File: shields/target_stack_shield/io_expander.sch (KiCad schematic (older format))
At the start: 21 parts, among them U5 PCA9535CPW,118

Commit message: work on target stack shield layout
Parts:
- C7: footprint (none) -> Capacitor_SMD:C_0603_1608Metric_Pad1.05x0.95mm_HandSolder
- JP1, JP2, JP3: footprint (none) -> Jumper:SolderJumper-2_P1.3mm_Open_TrianglePad1.0x1.5mm
- LED2: footprint KRTBAILMS15B5CB1B120R18 -> hive:KRTBAILMS15B5CB1B120R18
- R10, R11, R12, R13, R14, R15, R16, R2, R3, R4, R5, R6, R7, R8, R9: footprint (none) -> Resistor_SMD:R_0603_1608Metric_Pad1.05x0.95mm_HandSolder
- U5: footprint SOP65P640X110-24N -> hive:SOP65P640X110-24N
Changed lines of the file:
@@
 F 0 "U5" H 6000 4320 50  0000 C CNN
 F 1 "PCA9535CPW,118" H 6000 4229 50  0000 C CNN
-F 2 "SOP65P640X110-24N" H 6000 3150 50  0001 L BNN
+F 2 "hive:SOP65P640X110-24N" H 6000 3150 50  0001 L BNN
 F 3 "" H 6000 3150 50  0001 L BNN
 F 4 "70R6541" H 6000 3150 50  0001 L BNN "OC_NEWARK"
@@
 F 0 "JP1" H 1600 1355 50  0000 C CNN
 F 1 "Address Bit 0" H 1600 1264 50  0000 C CNN
-F 2 "" H 1600 1150 50  0001 C CNN
+F 2 "Jumper:SolderJumper-2_P1.3mm_Open_TrianglePad1.0x1.5mm" H 1600 1150 50  0001 C CNN
 F 3 "~" H 1600 1150 50  0001 C CNN
 	1    1600 1150
@@
 F 0 "JP2" H 1600 1755 50  0000 C CNN
 F 1 "Address Bit 1" H 1600 1664 50  0000 C CNN
-F 2 "" H 1600 1550 50  0001 C CNN
+F 2 "Jumper:SolderJumper-2_P1.3mm_Open_TrianglePad1.0x1.5mm" H 1600 1550 50  0001 C CNN
 F 3 "~" H 1600 1550 50  0001 C CNN
 	1    1600 1550
@@
 F 0 "JP3" H 1600 2155 50  0000 C CNN
 F 1 "Address Bit 2" H 1600 2064 50  0000 C CNN
-F 2 "" H 1600 1950 50  0001 C CNN
+F 2 "Jumper:SolderJumper-2_P1.3mm_Open_TrianglePad1.0x1.5mm" H 1600 1950 50  0001 C CNN
 F 3 "~" H 1600 1950 50  0001 C CNN
 	1    1600 1950
@@
 F 0 "R2" H 2209 2246 50  0000 L CNN
 F 1 "100k" H 2209 2155 50  0000 L CNN
-F 2 "" H 2150 2200 50  0001 C CNN
+F 2 "Resistor_SMD:R_0603_1608Metric_Pad1.05x0.95mm_HandSolder" H 2150 2200 50  0001 C CNN
 F 3 "~" H 2150 2200 50  0001 C CNN
 	1    2150 2200
@@
 F 0 "R3" H 2559 2246 50  0000 L CNN
 F 1 "100k" H 2559 2155 50  0000 L CNN
-F 2 "" H 2500 2200 50  0001 C CNN
+F 2 "Resistor_SMD:R_0603_1608Metric_Pad1.05x0.95mm_HandSolder" H 2500 2200 50  0001 C CNN
 F 3 "~" H 2500 2200 50  0001 C CNN
 	1    2500 2200
@@
 F 0 "R4" H 2909 2246 50  0000 L CNN
 F 1 "100k" H 2909 2155 50  0000 L CNN
-F 2 "" H 2850 2200 50  0001 C CNN
+F 2 "Resistor_SMD:R_0603_1608Metric_Pad1.05x0.95mm_HandSolder" H 2850 2200 50  0001 C CNN
 F 3 "~" H 2850 2200 50  0001 C CNN
 	1    2850 2200
@@
 F 0 "C7" H 5192 2196 50  0000 L CNN
 F 1 "100n" H 5192 2105 50  0000 L CNN
-F 2 "" H 5100 2150 50  0001 C CNN
+F 2 "Capacitor_SMD:C_0603_1608Metric_Pad1.05x0.95mm_HandSolder" H 5100 2150 50  0001 C CNN
 F 3 "~" H 5100 2150 50  0001 C CNN
 	1    5100 2150
@@
 F 0 "LED2" H 9350 1415 50  0000 C CNN
 F 1 "KRTB_AILMS1-5B5C-B1B12-0-R18" H 9350 1324 50  0000 C CNN
-F 2 "KRTBAILMS15B5CB1B120R18" H 9800 1250 50  0001 L CNN
+F 2 "hive:KRTBAILMS15B5CB1B120R18" H 9800 1250 50  0001 L CNN
 F 3 "" H 9800 1150 50  0001 L CNN
 F 4 "OSRAM OPTO SEMICONDUCTORS - KRTB AILMS1-5B5C-B1B12-0-R18 - LED, Red, Green, Blue, SMD, 120 , Rectangular, R 20mA, G 20mA, B 20mA" H 9800 1050 50  0001 L CNN "Description"
@@
 F 0 "R5" V 4750 3550 50  0000 L CNN
 F 1 "150" V 4750 2900 50  0000 L CNN
-F 2 "" H 4700 3250 50  0001 C CNN
+F 2 "Resistor_SMD:R_0603_1608Metric_Pad1.05x0.95mm_HandSolder" H 4700 3250 50  0001 C CNN
 F 3 "~" H 4700 3250 50  0001 C CNN
 	1    4700 3250
@@
 F 0 "R6" V 4750 3650 50  0000 L CNN
 F 1 "45" V 4750 3000 50  0000 L CNN
-F 2 "" H 4700 3350 50  0001 C CNN
+F 2 "Resistor_SMD:R_0603_1608Metric_Pad1.05x0.95mm_HandSolder" H 4700 3350 50  0001 C CNN
 F 3 "~" H 4700 3350 50  0001 C CNN
 	1    4700 3350
@@
 F 0 "R7" V 4750 3750 50  0000 L CNN
 F 1 "30" V 4750 3100 50  0000 L CNN
-F 2 "" H 4700 3450 50  0001 C CNN
+F 2 "Resistor_SMD:R_0603_1608Metric_Pad1.05x0.95mm_HandSolder" H 4700 3450 50  0001 C CNN
 F 3 "~" H 4700 3450 50  0001 C CNN
 	1    4700 3450
@@
 F 0 "R8" V 6850 3400 50  0000 L CNN
 F 1 "100k" V 6850 3850 50  0000 L CNN
-F 2 "" H 6900 3700 50  0001 C CNN
+F 2 "Resistor_SMD:R_0603_1608Metric_Pad1.05x0.95mm_HandSolder" H 6900 3700 50  0001 C CNN
 F 3 "~" H 6900 3700 50  0001 C CNN
 	1    6900 3700
@@
 F 0 "R9" V 7000 3400 50  0000 L CNN
 F 1 "100k" V 7000 3850 50  0000 L CNN
-F 2 "" H 7050 3700 50  0001 C CNN
+F 2 "Resistor_SMD:R_0603_1608Metric_Pad1.05x0.95mm_HandSolder" H 7050 3700 50  0001 C CNN
 F 3 "~" H 7050 3700 50  0001 C CNN
 	1    7050 3700
@@
 F 0 "R10" V 7150 3400 50  0000 L CNN
 F 1 "100k" V 7150 3850 50  0000 L CNN
-F 2 "" H 7200 3700 50  0001 C CNN
+F 2 "Resistor_SMD:R_0603_1608Metric_Pad1.05x0.95mm_HandSolder" H 7200 3700 50  0001 C CNN
 F 3 "~" H 7200 3700 50  0001 C CNN
 	1    7200 3700
@@
 F 0 "R11" V 7300 3400 50  0000 L CNN
 F 1 "100k" V 7300 3850 50  0000 L CNN
-F 2 "" H 7350 3700 50  0001 C CNN
+F 2 "Resistor_SMD:R_0603_1608Metric_Pad1.05x0.95mm_HandSolder" H 7350 3700 50  0001 C CNN
 F 3 "~" H 7350 3700 50  0001 C CNN
 	1    7350 3700
@@
 F 0 "R12" V 7450 3400 50  0000 L CNN
 F 1 "100k" V 7450 3850 50  0000 L CNN
-F 2 "" H 7500 3700 50  0001 C CNN
+F 2 "Resistor_SMD:R_0603_1608Metric_Pad1.05x0.95mm_HandSolder" H 7500 3700 50  0001 C CNN
 F 3 "~" H 7500 3700 50  0001 C CNN
 	1    7500 3700
@@
 F 0 "R13" V 7600 3400 50  0000 L CNN
 F 1 "100k" V 7600 3850 50  0000 L CNN
-F 2 "" H 7650 3700 50  0001 C CNN
+F 2 "Resistor_SMD:R_0603_1608Metric_Pad1.05x0.95mm_HandSolder" H 7650 3700 50  0001 C CNN
 F 3 "~" H 7650 3700 50  0001 C CNN
 	1    7650 3700
@@
 F 0 "R14" V 7750 3400 50  0000 L CNN
 F 1 "100k" V 7750 3850 50  0000 L CNN
-F 2 "" H 7800 3700 50  0001 C CNN
+F 2 "Resistor_SMD:R_0603_1608Metric_Pad1.05x0.95mm_HandSolder" H 7800 3700 50  0001 C CNN
 F 3 "~" H 7800 3700 50  0001 C CNN
 	1    7800 3700
@@
 F 0 "R15" V 7900 3400 50  0000 L CNN
 F 1 "100k" V 7900 3850 50  0000 L CNN
-F 2 "" H 7950 3700 50  0001 C CNN
+F 2 "Resistor_SMD:R_0603_1608Metric_Pad1.05x0.95mm_HandSolder" H 7950 3700 50  0001 C CNN
 F 3 "~" H 7950 3700 50  0001 C CNN
 	1    7950 3700
@@
 F 0 "R16" V 4350 3650 50  0000 L CNN
 F 1 "100k" V 4350 4100 50  0000 L CNN
-F 2 "" H 4400 3950 50  0001 C CNN
+F 2 "Resistor_SMD:R_0603_1608Metric_Pad1.05x0.95mm_HandSolder" H 4400 3950 50  0001 C CNN
 F 3 "~" H 4400 3950 50  0001 C CNN
 	1    4400 3950

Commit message: Further work on layout
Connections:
- net BUS_SW_CH0: now also R15.1, U5.20 (IO1_7); no longer R8.1, U5.13 (IO1_0)
- net BUS_SW_CH1: now also R14.1, U5.19 (IO1_6); no longer R9.1, U5.14 (IO1_1)
- net BUS_SW_CH2: now also R13.1, U5.18 (IO1_5); no longer R10.1, U5.15 (IO1_2)
- net BUS_SW_CH3: now also R12.1, U5.17 (IO1_4); no longer R11.1, U5.16 (IO1_3)
- net TARGET_SW_CH0: now also R11.1, U5.16 (IO1_3); no longer R12.1, U5.17 (IO1_4)
- net TARGET_SW_CH1: now also R10.1, U5.15 (IO1_2); no longer R13.1, U5.18 (IO1_5)
- net TARGET_SW_CH2: now also R9.1, U5.14 (IO1_1); no longer R14.1, U5.19 (IO1_6)
- net TARGET_SW_CH3: now also R8.1, U5.13 (IO1_0); no longer R15.1, U5.20 (IO1_7)
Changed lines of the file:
@@
 	1    0    0    -1
 $EndComp
-Text HLabel 8700 2550 2    50   Output ~ 0
+Text HLabel 8700 3250 2    50   Output ~ 0
 BUS_SW_CH0
 Connection ~ 7200 2750
 Wire Wire Line
 	7200 2750 8700 2750
+Text HLabel 8700 3150 2    50   Output ~ 0
+BUS_SW_CH1
+Text HLabel 8700 3050 2    50   Output ~ 0
+BUS_SW_CH2
+Text HLabel 8700 2950 2    50   Output ~ 0
+BUS_SW_CH3
+Text HLabel 8700 2850 2    50   Output ~ 0
+TARGET_SW_CH0
+Text HLabel 8700 2750 2    50   Output ~ 0
+TARGET_SW_CH1
 Text HLabel 8700 2650 2    50   Output ~ 0
-BUS_SW_CH1
-Text HLabel 8700 2750 2    50   Output ~ 0
-BUS_SW_CH2
-Text HLabel 8700 2850 2    50   Output ~ 0
-BUS_SW_CH3
-Text HLabel 8700 2950 2    50   Output ~ 0
-TARGET_SW_CH0
-Text HLabel 8700 3050 2    50   Output ~ 0
-TARGET_SW_CH1
-Text HLabel 8700 3150 2    50   Output ~ 0
 TARGET_SW_CH2
-Text HLabel 8700 3250 2    50   Output ~ 0
+Text HLabel 8700 2550 2    50   Output ~ 0
 TARGET_SW_CH3
 Wire Wire Line

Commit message: added partlist and prices
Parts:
- JP1, JP2, JP3, R10, R11, R12, R13, R14, R15, R16, R2, R3, R4, R5, R6, R7, R8, R9: Digikey Price (CHF) (none) -> -; Mouser Price (CHF) (none) -> -
- LED2: Digikey Price (CHF) (none) -> 0.38; Mouser Price (CHF) (none) -> 0.38
- U5: Digikey Price (CHF) (none) -> 1.9; Mouser Price (CHF) (none) -> 1.92
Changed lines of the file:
@@
 F 7 "NXP" H 6000 3150 50  0001 L BNN "SUPPLIER"
 F 8 "-" H 6000 3150 50  0001 L BNN "OC_FARNELL"
+F 9 "1.9" H 6000 3150 50  0001 C CNN "Digikey Price (CHF)"
+F 10 "1.92" H 6000 3150 50  0001 C CNN "Mouser Price (CHF)"
 	1    6000 3150
 	1    0    0    -1
@@
 F 2 "Jumper:SolderJumper-2_P1.3mm_Open_TrianglePad1.0x1.5mm" H 1600 1150 50  0001 C CNN
 F 3 "~" H 1600 1150 50  0001 C CNN
+F 4 "-" H 1600 1150 50  0001 C CNN "Digikey Price (CHF)"
+F 5 "-" H 1600 1150 50  0001 C CNN "Mouser Price (CHF)"
 	1    1600 1150
 	1    0    0    -1
@@
 F 2 "Jumper:SolderJumper-2_P1.3mm_Open_TrianglePad1.0x1.5mm" H 1600 1550 50  0001 C CNN
 F 3 "~" H 1600 1550 50  0001 C CNN
+F 4 "-" H 1600 1550 50  0001 C CNN "Digikey Price (CHF)"
+F 5 "-" H 1600 1550 50  0001 C CNN "Mouser Price (CHF)"
 	1    1600 1550
 	1    0    0    -1
@@
 F 2 "Jumper:SolderJumper-2_P1.3mm_Open_TrianglePad1.0x1.5mm" H 1600 1950 50  0001 C CNN
 F 3 "~" H 1600 1950 50  0001 C CNN
+F 4 "-" H 1600 1950 50  0001 C CNN "Digikey Price (CHF)"
+F 5 "-" H 1600 1950 50  0001 C CNN "Mouser Price (CHF)"
 	1    1600 1950
 	1    0    0    -1
@@
 F 2 "Resistor_SMD:R_0603_1608Metric_Pad1.05x0.95mm_HandSolder" H 2150 2200 50  0001 C CNN
 F 3 "~" H 2150 2200 50  0001 C CNN
+F 4 "-" H 2150 2200 50  0001 C CNN "Digikey Price (CHF)"
+F 5 "-" H 2150 2200 50  0001 C CNN "Mouser Price (CHF)"
 	1    2150 2200
 	1    0    0    -1
@@
 F 2 "Resistor_SMD:R_0603_1608Metric_Pad1.05x0.95mm_HandSolder" H 2500 2200 50  0001 C CNN
 F 3 "~" H 2500 2200 50  0001 C CNN
+F 4 "-" H 2500 2200 50  0001 C CNN "Digikey Price (CHF)"
+F 5 "-" H 2500 2200 50  0001 C CNN "Mouser Price (CHF)"
 	1    2500 2200
 	1    0    0    -1
@@
 F 2 "Resistor_SMD:R_0603_1608Metric_Pad1.05x0.95mm_HandSolder" H 2850 2200 50  0001 C CNN
 F 3 "~" H 2850 2200 50  0001 C CNN
+F 4 "-" H 2850 2200 50  0001 C CNN "Digikey Price (CHF)"
+F 5 "-" H 2850 2200 50  0001 C CNN "Mouser Price (CHF)"
 	1    2850 2200
 	1    0    0    -1
@@
 F 8 "OSRAM" H 9800 650 50  0001 L CNN "Manufacturer_Name"
 F 9 "KRTB AILMS1-5B5C-B1B12-0-R18" H 9800 550 50  0001 L CNN "Manufacturer_Part_Number"
+F 10 "0.38" H 8750 1150 50  0001 C CNN "Digikey Price (CHF)"
+F 11 "0.38" H 8750 1150 50  0001 C CNN "Mouser Price (CHF)"
 	1    8750 1150
 	1    0    0    -1
@@
 F 2 "Resistor_SMD:R_0603_1608Metric_Pad1.05x0.95mm_HandSolder" H 4700 3250 50  0001 C CNN
 F 3 "~" H 4700 3250 50  0001 C CNN
+F 4 "-" H 4700 3250 50  0001 C CNN "Digikey Price (CHF)"
+F 5 "-" H 4700 3250 50  0001 C CNN "Mouser Price (CHF)"
 	1    4700 3250
 	0    -1   -1   0
@@
 F 2 "Resistor_SMD:R_0603_1608Metric_Pad1.05x0.95mm_HandSolder" H 4700 3350 50  0001 C CNN
 F 3 "~" H 4700 3350 50  0001 C CNN
+F 4 "-" H 4700 3350 50  0001 C CNN "Digikey Price (CHF)"
+F 5 "-" H 4700 3350 50  0001 C CNN "Mouser Price (CHF)"
 	1    4700 3350
 	0    -1   -1   0
@@
 F 2 "Resistor_SMD:R_0603_1608Metric_Pad1.05x0.95mm_HandSolder" H 4700 3450 50  0001 C CNN
 F 3 "~" H 4700 3450 50  0001 C CNN
+F 4 "-" H 4700 3450 50  0001 C CNN "Digikey Price (CHF)"
+F 5 "-" H 4700 3450 50  0001 C CNN "Mouser Price (CHF)"
 	1    4700 3450
 	0    -1   -1   0
@@
 F 2 "Resistor_SMD:R_0603_1608Metric_Pad1.05x0.95mm_HandSolder" H 6900 3700 50  0001 C CNN
 F 3 "~" H 6900 3700 50  0001 C CNN
+F 4 "-" H 6900 3700 50  0001 C CNN "Digikey Price (CHF)"
+F 5 "-" H 6900 3700 50  0001 C CNN "Mouser Price (CHF)"
 	1    6900 3700
 	1    0    0    -1
@@
 F 2 "Resistor_SMD:R_0603_1608Metric_Pad1.05x0.95mm_HandSolder" H 7050 3700 50  0001 C CNN
 F 3 "~" H 7050 3700 50  0001 C CNN
+F 4 "-" H 7050 3700 50  0001 C CNN "Digikey Price (CHF)"
+F 5 "-" H 7050 3700 50  0001 C CNN "Mouser Price (CHF)"
 	1    7050 3700
 	1    0    0    -1
@@
 F 2 "Resistor_SMD:R_0603_1608Metric_Pad1.05x0.95mm_HandSolder" H 7200 3700 50  0001 C CNN
 F 3 "~" H 7200 3700 50  0001 C CNN
+F 4 "-" H 7200 3700 50  0001 C CNN "Digikey Price (CHF)"
+F 5 "-" H 7200 3700 50  0001 C CNN "Mouser Price (CHF)"
 	1    7200 3700
 	1    0    0    -1
@@
 F 2 "Resistor_SMD:R_0603_1608Metric_Pad1.05x0.95mm_HandSolder" H 7350 3700 50  0001 C CNN
 F 3 "~" H 7350 3700 50  0001 C CNN
+F 4 "-" H 7350 3700 50  0001 C CNN "Digikey Price (CHF)"
+F 5 "-" H 7350 3700 50  0001 C CNN "Mouser Price (CHF)"
 	1    7350 3700
 	1    0    0    -1
@@
 F 2 "Resistor_SMD:R_0603_1608Metric_Pad1.05x0.95mm_HandSolder" H 7500 3700 50  0001 C CNN
 F 3 "~" H 7500 3700 50  0001 C CNN
+F 4 "-" H 7500 3700 50  0001 C CNN "Digikey Price (CHF)"
+F 5 "-" H 7500 3700 50  0001 C CNN "Mouser Price (CHF)"
 	1    7500 3700
 	1    0    0    -1
@@
 F 2 "Resistor_SMD:R_0603_1608Metric_Pad1.05x0.95mm_HandSolder" H 7650 3700 50  0001 C CNN
 F 3 "~" H 7650 3700 50  0001 C CNN
+F 4 "-" H 7650 3700 50  0001 C CNN "Digikey Price (CHF)"
+F 5 "-" H 7650 3700 50  0001 C CNN "Mouser Price (CHF)"
 	1    7650 3700
 	1    0    0    -1
@@
 F 2 "Resistor_SMD:R_0603_1608Metric_Pad1.05x0.95mm_HandSolder" H 7800 3700 50  0001 C CNN
 F 3 "~" H 7800 3700 50  0001 C CNN
+F 4 "-" H 7800 3700 50  0001 C CNN "Digikey Price (CHF)"
+F 5 "-" H 7800 3700 50  0001 C CNN "Mouser Price (CHF)"
 	1    7800 3700
 	1    0    0    -1
@@
 F 2 "Resistor_SMD:R_0603_1608Metric_Pad1.05x0.95mm_HandSolder" H 7950 3700 50  0001 C CNN
 F 3 "~" H 7950 3700 50  0001 C CNN
+F 4 "-" H 7950 3700 50  0001 C CNN "Digikey Price (CHF)"
+F 5 "-" H 7950 3700 50  0001 C CNN "Mouser Price (CHF)"
 	1    7950 3700
 	1    0    0    -1
@@
 F 2 "Resistor_SMD:R_0603_1608Metric_Pad1.05x0.95mm_HandSolder" H 4400 3950 50  0001 C CNN
 F 3 "~" H 4400 3950 50  0001 C CNN
+F 4 "-" H 4400 3950 50  0001 C CNN "Digikey Price (CHF)"
+F 5 "-" H 4400 3950 50  0001 C CNN "Mouser Price (CHF)"
 	1    4400 3950
 	1    0    0    -1

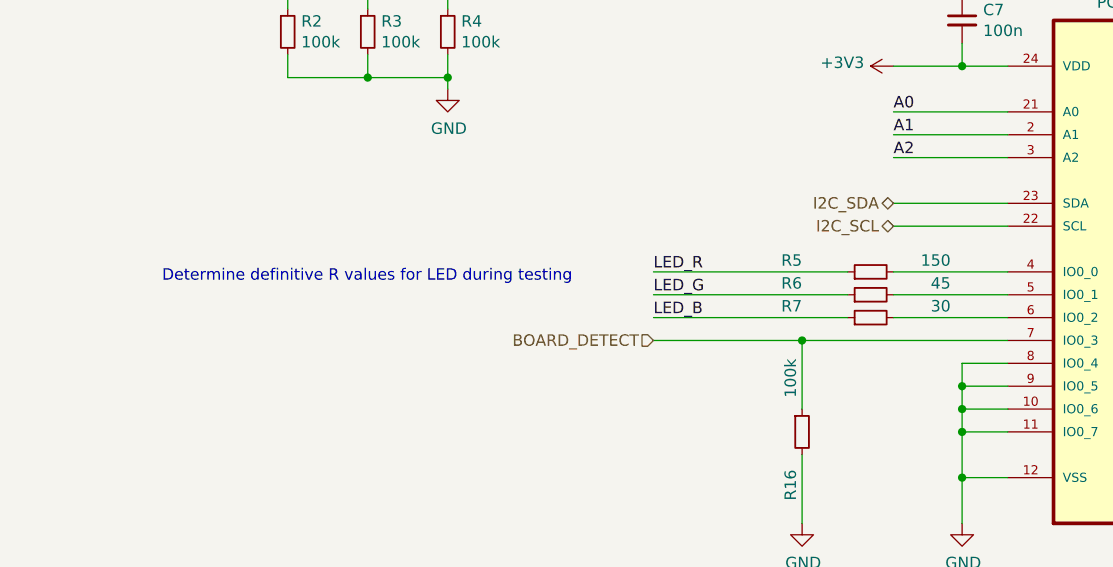
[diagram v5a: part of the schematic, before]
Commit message: added definitive led resistor values
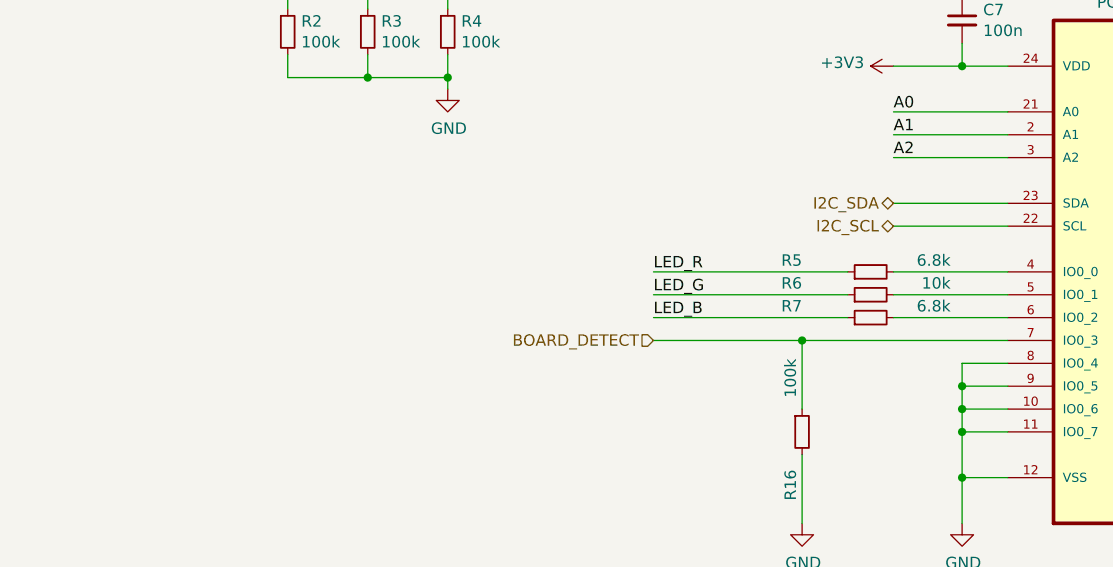
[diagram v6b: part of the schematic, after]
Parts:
- R5: value 150 -> 6.8k
- R6: value 45 -> 10k
- R7: value 30 -> 6.8k
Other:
- note removed: "Determine definitive R values for LED during testing"
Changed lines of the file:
@@
 P 4700 3250
 F 0 "R5" V 4750 3550 50  0000 L CNN
-F 1 "150" V 4750 2900 50  0000 L CNN
+F 1 "6.8k" V 4750 2900 50  0000 L CNN
 F 2 "Resistor_SMD:R_0603_1608Metric_Pad1.05x0.95mm_HandSolder" H 4700 3250 50  0001 C CNN
 F 3 "~" H 4700 3250 50  0001 C CNN
@@
 P 4700 3350
 F 0 "R6" V 4750 3650 50  0000 L CNN
-F 1 "45" V 4750 3000 50  0000 L CNN
+F 1 "10k" V 4750 3000 50  0000 L CNN
 F 2 "Resistor_SMD:R_0603_1608Metric_Pad1.05x0.95mm_HandSolder" H 4700 3350 50  0001 C CNN
 F 3 "~" H 4700 3350 50  0001 C CNN
@@
 P 4700 3450
 F 0 "R7" V 4750 3750 50  0000 L CNN
-F 1 "30" V 4750 3100 50  0000 L CNN
+F 1 "6.8k" V 4750 3100 50  0000 L CNN
 F 2 "Resistor_SMD:R_0603_1608Metric_Pad1.05x0.95mm_HandSolder" H 4700 3450 50  0001 C CNN
 F 3 "~" H 4700 3450 50  0001 C CNN
@@
 	5100 3650 5100 3750
 Connection ~ 5100 3750
-Text Notes 1600 3300 0    50   ~ 0
-Determine definitive R values for LED during testing
 Wire Wire Line
 	6700 2350 6800 2350
